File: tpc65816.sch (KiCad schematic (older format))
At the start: 33 parts, among them J1 Barrel_Jack, SW1 RESET, SW2 SW_SPDT, U1 74HC00, U2 74LS245, U3 WD65C816S, U4 L7805, U5 74LS573, U6 IS61C5128AS-25QLI, U7 28C256

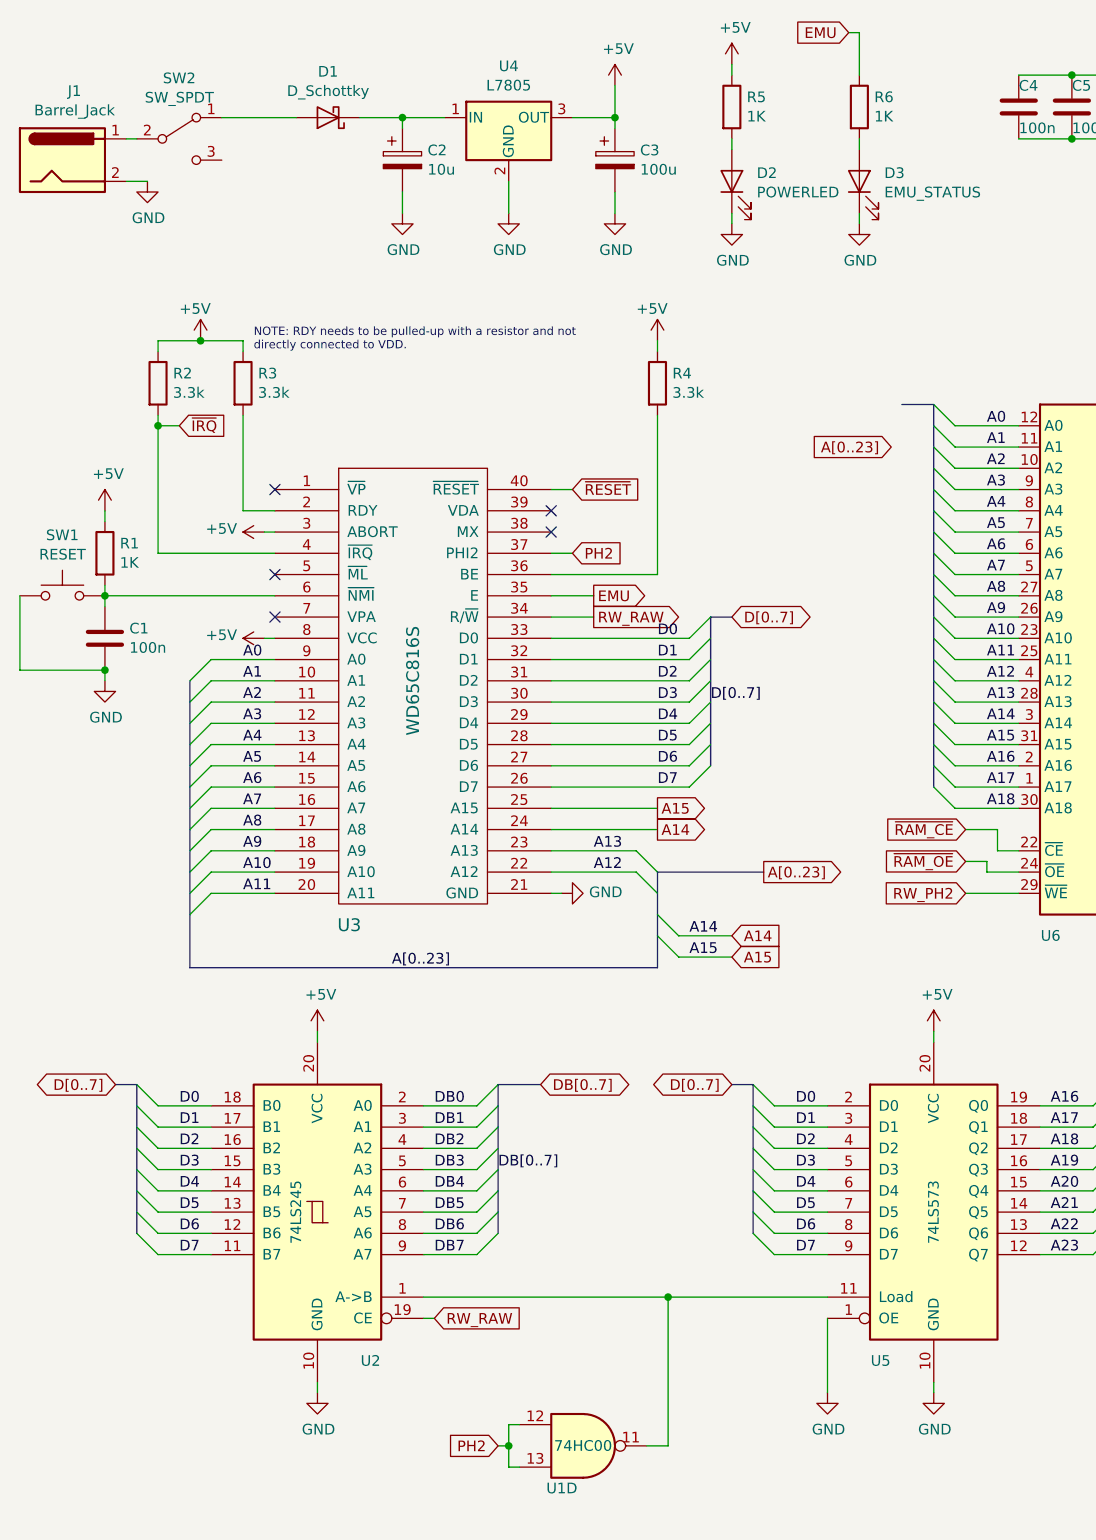
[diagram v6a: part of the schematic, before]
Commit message: Fix for bank decoder logic
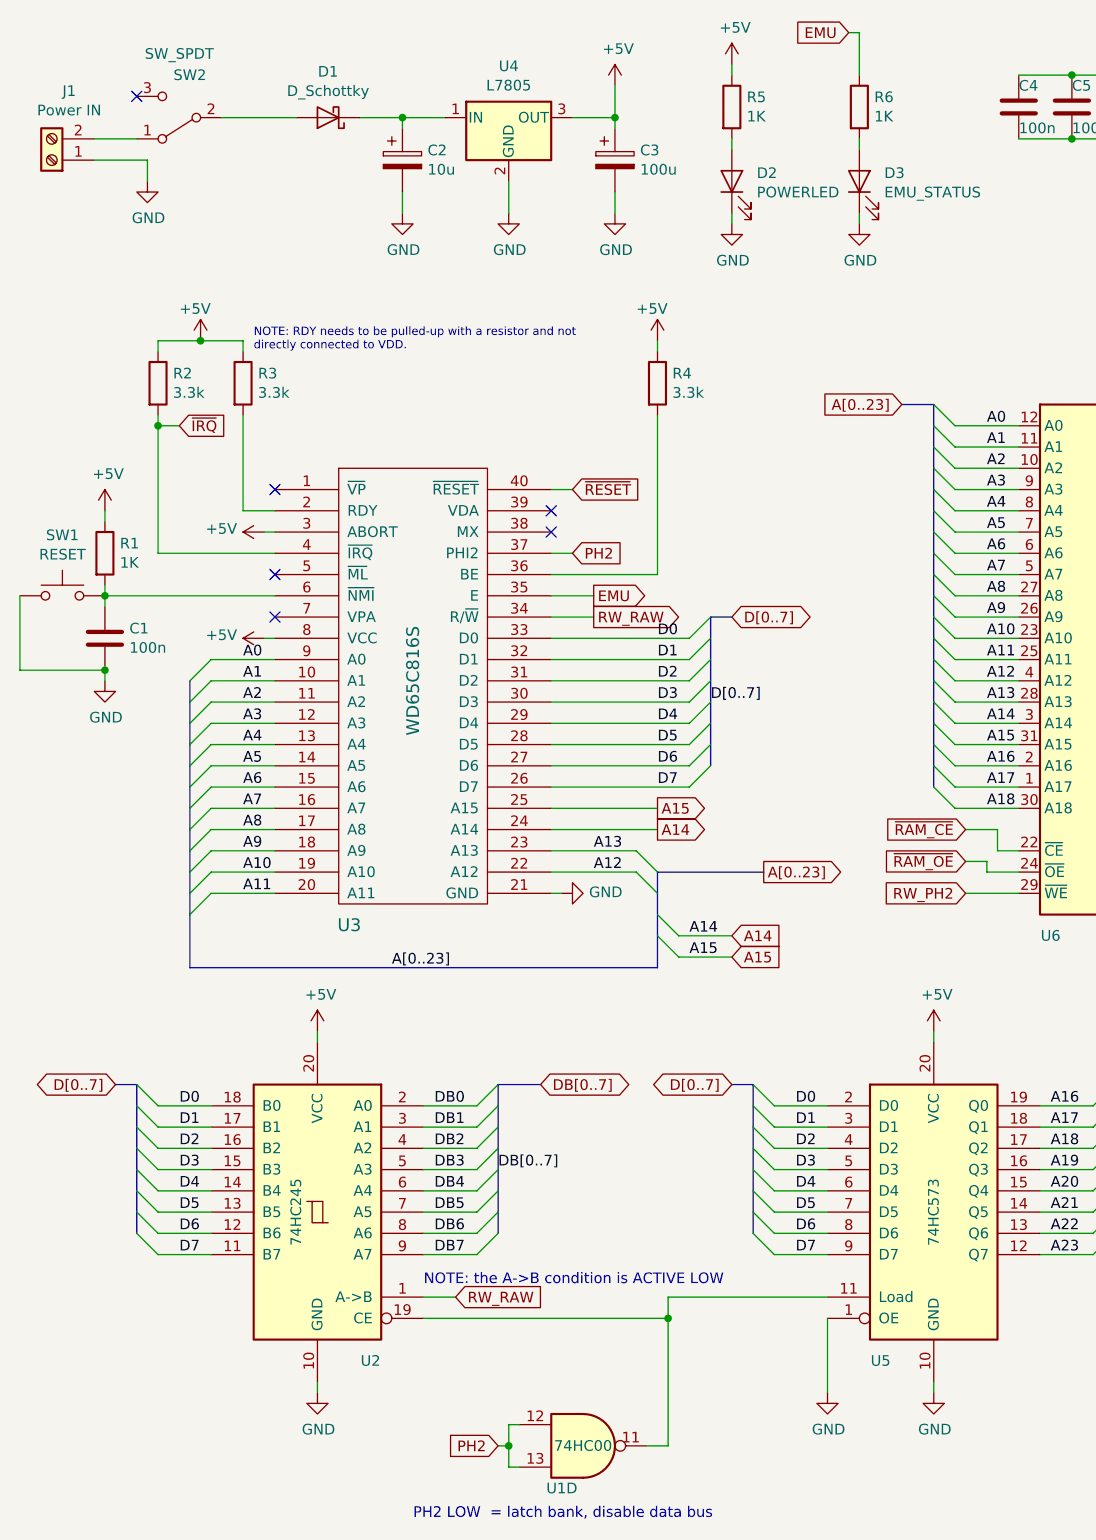
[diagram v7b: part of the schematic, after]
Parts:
- removed J1: Barrel_Jack, Connector_BarrelJack:BarrelJack_Horizontal, symbol Connector:Barrel_Jack
- added J1: Power IN, TerminalBlock:TerminalBlock_bornier-2_P5.08mm, symbol Connector:Screw_Terminal_01x02
- U2: value 74LS245 -> 74HC245
- U4: footprint Package_TO_SOT_THT:TO-220-3_Horizontal_TabDown -> Package_TO_SOT_THT:TO-220F-3_Horizontal_TabDown
- U5: value 74LS573 -> 74HC573
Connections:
- net GND: now also J1.1 (Pin_1)
- net RW_RAW: now also U2.1 (A->B); no longer U2.19 (CE)
- net at D1.2 (A): now also SW2.2 (B); no longer SW2.1 (A)
- net at U1.11, U5.11 (Load): now also U2.19 (CE); no longer U2.1 (A->B)
- new net: J1.2 (Pin_2), SW2.1 (A)
- no-connect marks 18 -> 19
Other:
- note added: "NOTE: the A->B condition is ACTIVE LOW"
- note added: "PH2 LOW = latch bank, disable data bus"
- moved on the sheet: SW2
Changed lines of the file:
@@
 F 0 "U4" H 3000 1242 50  0000 C CNN
 F 1 "L7805" H 3000 1151 50  0000 C CNN
-F 2 "Package_TO_SOT_THT:TO-220-3_Horizontal_TabDown" H 3025 850 50  0001 L CIN
+F 2 "Package_TO_SOT_THT:TO-220F-3_Horizontal_TabDown" H 3025 850 50  0001 L CIN
 F 3 "http://www.st.com/content/ccc/resource/technical/document/datasheet/41/4f/b3/b0/12/d4/47/88/CD00000444.pdf/files/CD00000444.pdf/jcr:content/translations/en.CD00000444.pdf" H 3000 950 50  0001 C CNN
 	1    3000 1000
@@
 Connection ~ 2500 1000
 $Comp
-L Connector:Barrel_Jack J1
-U 1 1 5FB9B723
-P 900 1200
-F 0 "J1" H 957 1525 50  0000 C CNN
-F 1 "Barrel_Jack" H 957 1434 50  0000 C CNN
-F 2 "Connector_BarrelJack:BarrelJack_Horizontal" H 950 1160 50  0001 C CNN
-F 3 "~" H 950 1160 50  0001 C CNN
-	1    900  1200
-	1    0    0    -1
-$EndComp
-$Comp
 L 74xx:74LS573 U5
 U 1 1 5FBAD8B1
 P 5000 6150
 F 0 "U5" H 4750 5450 50  0000 C CNN
-F 1 "74LS573" V 5000 6150 50  0000 C CNN
+F 1 "74HC573" V 5000 6150 50  0000 C CNN
 F 2 "Package_SO:SOIC-20W_7.5x12.8mm_P1.27mm" H 5000 6150 50  0001 C CNN
 F 3 "74xx/74hc573.pdf" H 5000 6150 50  0001 C CNN
@@
 P 2100 6150
 F 0 "U2" H 1850 5450 50  0000 C CNN
-F 1 "74LS245" V 2200 6150 50  0000 C CNN
+F 1 "74HC245" V 2200 6150 50  0000 C CNN
 F 2 "Package_SO:SOIC-20W_7.5x12.8mm_P1.27mm" H 2100 6150 50  0001 C CNN
 F 3 "http://www.ti.com/lit/gpn/sn74LS245" H 2100 6150 50  0001 C CNN
@@
 Wire Bus Line
 	5000 2350 4850 2350
-Text GLabel 4800 2550 0    50   Input ~ 0
+Text GLabel 4850 2350 0    50   Input ~ 0
 A[0..23]
 Text GLabel 3700 4350 2    50   Output ~ 0
@@
 	6650 800  6400 800
 Connection ~ 6400 800
-Text GLabel 2650 6650 2    50   Input ~ 0
+Text GLabel 2750 6550 2    50   Input ~ 0
 RW_RAW
 $Sheet
@@
 	4500 6550 3750 6550
 Wire Wire Line
-	3750 6550 3750 7250
+	3750 6550 3750 6650
 $Comp
 L power:+5V #PWR025
@@
 Text GLabel 1450 2450 2    50   Input ~ 0
 ~IRQ
-$Comp
-L Switch:SW_SPDT SW2
-U 1 1 5FEC970D
-P 1450 1100
-F 0 "SW2" H 1450 1385 50  0000 C CNN
-F 1 "SW_SPDT" H 1450 1294 50  0000 C CNN
-F 2 "slide_switch:spdt_slide_switch" H 1450 1100 50  0001 C CNN
-F 3 "~" H 1450 1100 50  0001 C CNN
-	1    1450 1100
-	1    0    0    -1
-$EndComp
 Wire Wire Line
 	1650 1000 2000 1000
 Wire Wire Line
-	1200 1100 1250 1100
+	1350 3050 1900 3050
+Wire Wire Line
+	1350 2450 1350 3050
+$Comp
+L Device:R R3
+U 1 1 5FC7A9F9
+P 1750 2250
+F 0 "R3" H 1820 2296 50  0000 L CNN
+F 1 "3.3k" H 1820 2205 50  0000 L CNN
+F 2 "Resistor_SMD:R_1206_3216Metric_Pad1.42x1.75mm_HandSolder" V 1680 2250 50  0001 C CNN
+F 3 "~" H 1750 2250 50  0001 C CNN
+	1    1750 2250
+	1    0    0    -1
+$EndComp
+Wire Wire Line
+	1350 2050 1550 2050
+Wire Wire Line
+	1750 2050 1750 2100
+Wire Wire Line
+	1750 2400 1750 2850
+Wire Wire Line
+	1750 2850 1900 2850
+Connection ~ 1550 2050
+Wire Wire Line
+	1550 2050 1750 2050
+$Comp
+L Device:R R4
+U 1 1 5FCBE765
+P 3700 2250
+F 0 "R4" H 3770 2296 50  0000 L CNN
+F 1 "3.3k" H 3770 2205 50  0000 L CNN
+F 2 "Resistor_SMD:R_1206_3216Metric_Pad1.42x1.75mm_HandSolder" V 3630 2250 50  0001 C CNN
+F 3 "~" H 3700 2250 50  0001 C CNN
+	1    3700 2250
+	1    0    0    -1
+$EndComp
+$Comp
+L power:+5V #PWR014
+U 1 1 5FCBEE39
+P 3700 2050
+F 0 "#PWR014" H 3700 1900 50  0001 C CNN
+F 1 "+5V" H 3600 2200 50  0000 L CNN
+F 2 "" H 3700 2050 50  0001 C CNN
+F 3 "" H 3700 2050 50  0001 C CNN
+	1    3700 2050
+	1    0    0    -1
+$EndComp
+Wire Wire Line
+	3700 2050 3700 2100
+Wire Wire Line
+	3700 3150 3700 2400
+Wire Wire Line
+	3200 3150 3700 3150
+Text Notes 1800 2100 0    39   ~ 0
+NOTE: RDY needs to be pulled-up with a resistor and not \ndirectly connected to VDD.
+Wire Wire Line
+	3650 7250 3750 7250
+Text Notes 2600 6500 0    50   ~ 0
+NOTE: the A->B condition is ACTIVE LOW
+NoConn ~ 1250 900
+$Comp
+L Connector:Screw_Terminal_01x02 J1
+U 1 1 5FC8692F
+P 850 1200
+F 0 "J1" H 768 875 50  0000 C CNN
+F 1 "Power IN" H 768 966 50  0000 C CNN
+F 2 "TerminalBlock:TerminalBlock_bornier-2_P5.08mm" H 850 1200 50  0001 C CNN
+F 3 "~" H 850 1200 50  0001 C CNN
+	1    850  1200
+	-1   0    0    1
+$EndComp
+Wire Wire Line
+	1050 1100 1250 1100
 $Comp
 L power:GND #PWR03
@@
 	1    0    0    -1
 $EndComp
-Wire Wire Line
-	1200 1300 1300 1300
-Wire Wire Line
-	1350 3050 1900 3050
-Wire Wire Line
-	1350 2450 1350 3050
-$Comp
-L Device:R R3
-U 1 1 5FC7A9F9
-P 1750 2250
-F 0 "R3" H 1820 2296 50  0000 L CNN
-F 1 "3.3k" H 1820 2205 50  0000 L CNN
-F 2 "Resistor_SMD:R_1206_3216Metric_Pad1.42x1.75mm_HandSolder" V 1680 2250 50  0001 C CNN
-F 3 "~" H 1750 2250 50  0001 C CNN
-	1    1750 2250
-	1    0    0    -1
-$EndComp
-Wire Wire Line
-	1350 2050 1550 2050
-Wire Wire Line
-	1750 2050 1750 2100
-Wire Wire Line
-	1750 2400 1750 2850
-Wire Wire Line
-	1750 2850 1900 2850
-Connection ~ 1550 2050
-Wire Wire Line
-	1550 2050 1750 2050
-$Comp
-L Device:R R4
-U 1 1 5FCBE765
-P 3700 2250
-F 0 "R4" H 3770 2296 50  0000 L CNN
-F 1 "3.3k" H 3770 2205 50  0000 L CNN
-F 2 "Resistor_SMD:R_1206_3216Metric_Pad1.42x1.75mm_HandSolder" V 3630 2250 50  0001 C CNN
-F 3 "~" H 3700 2250 50  0001 C CNN
-	1    3700 2250
-	1    0    0    -1
-$EndComp
-$Comp
-L power:+5V #PWR014
-U 1 1 5FCBEE39
-P 3700 2050
-F 0 "#PWR014" H 3700 1900 50  0001 C CNN
-F 1 "+5V" H 3600 2200 50  0000 L CNN
-F 2 "" H 3700 2050 50  0001 C CNN
-F 3 "" H 3700 2050 50  0001 C CNN
-	1    3700 2050
-	1    0    0    -1
-$EndComp
-Wire Wire Line
-	3700 2050 3700 2100
-Wire Wire Line
-	3700 3150 3700 2400
-Wire Wire Line
-	3200 3150 3700 3150
-Text Notes 1800 2100 0    39   ~ 0
-NOTE: RDY needs to be pulled-up with a resistor and not \ndirectly connected to VDD.
-Wire Wire Line
-	2650 6650 2600 6650
-Wire Wire Line
-	3750 6550 2600 6550
-Connection ~ 3750 6550
-Wire Wire Line
-	3650 7250 3750 7250
+$Comp
+L Switch:SW_SPDT SW2
+U 1 1 5FEC970D
+P 1450 1000
+F 0 "SW2" H 1400 800 50  0000 C CNN
+F 1 "SW_SPDT" H 1450 700 50  0000 C CNN
+F 2 "slide_switch:spdt_slide_switch" H 1450 1000 50  0001 C CNN
+F 3 "~" H 1450 1000 50  0001 C CNN
+	1    1450 1000
+	-1   0    0    1
+$EndComp
+Wire Wire Line
+	1050 1200 1300 1200
+Wire Wire Line
+	1300 1200 1300 1300
+Wire Wire Line
+	2750 6550 2600 6550
+Wire Wire Line
+	2600 6650 3750 6650
+Connection ~ 3750 6650
+Wire Wire Line
+	3750 6650 3750 7250
+Text Notes 2550 7600 0    50   ~ 0
+PH2 LOW  = latch bank, disable data bus
 Wire Bus Line
 	10950 5150 10950 5450
